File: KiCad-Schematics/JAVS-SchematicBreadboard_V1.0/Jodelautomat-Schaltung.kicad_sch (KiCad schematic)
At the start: 63 parts, among them J1 AudioJack3, J2 I2C_5V_01x04, J4 Screw_Terminal_01x02, J5 USART_Full_01x06, Q1 BC337, Q2 BC337, Q3 BC337, Q4 BC337, Q5 BC337, Q6 BC337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

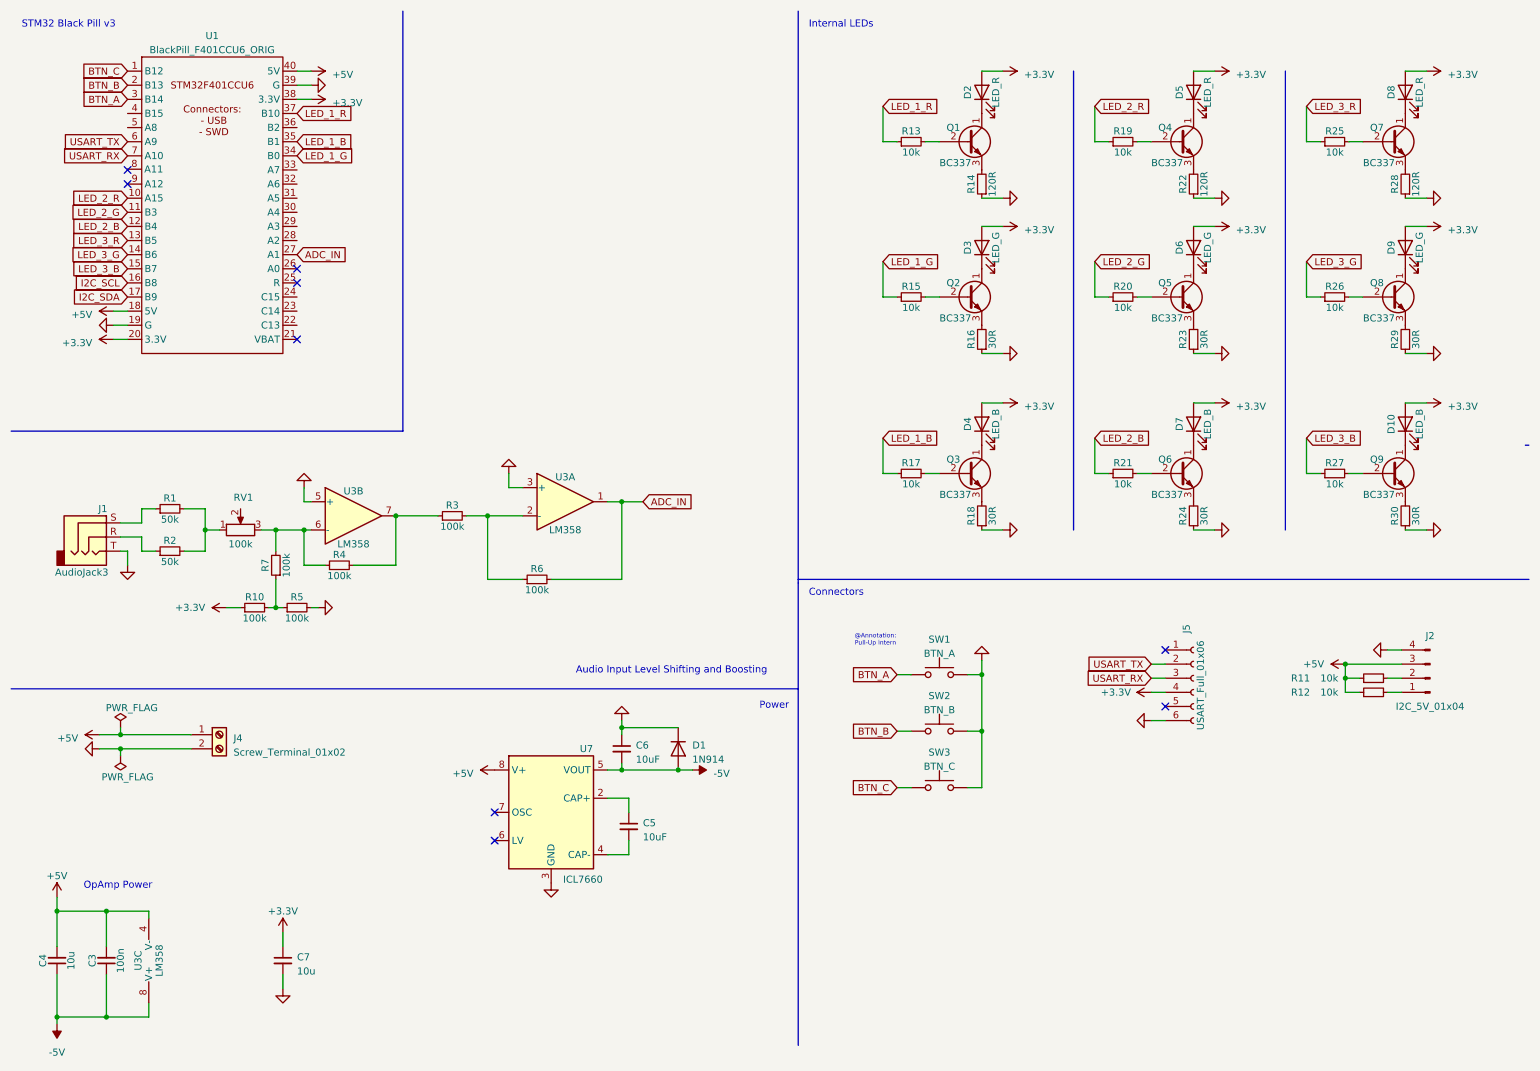
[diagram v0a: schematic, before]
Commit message: some modifications for breadboard creation; removed onboard leds for all stips except strip 1
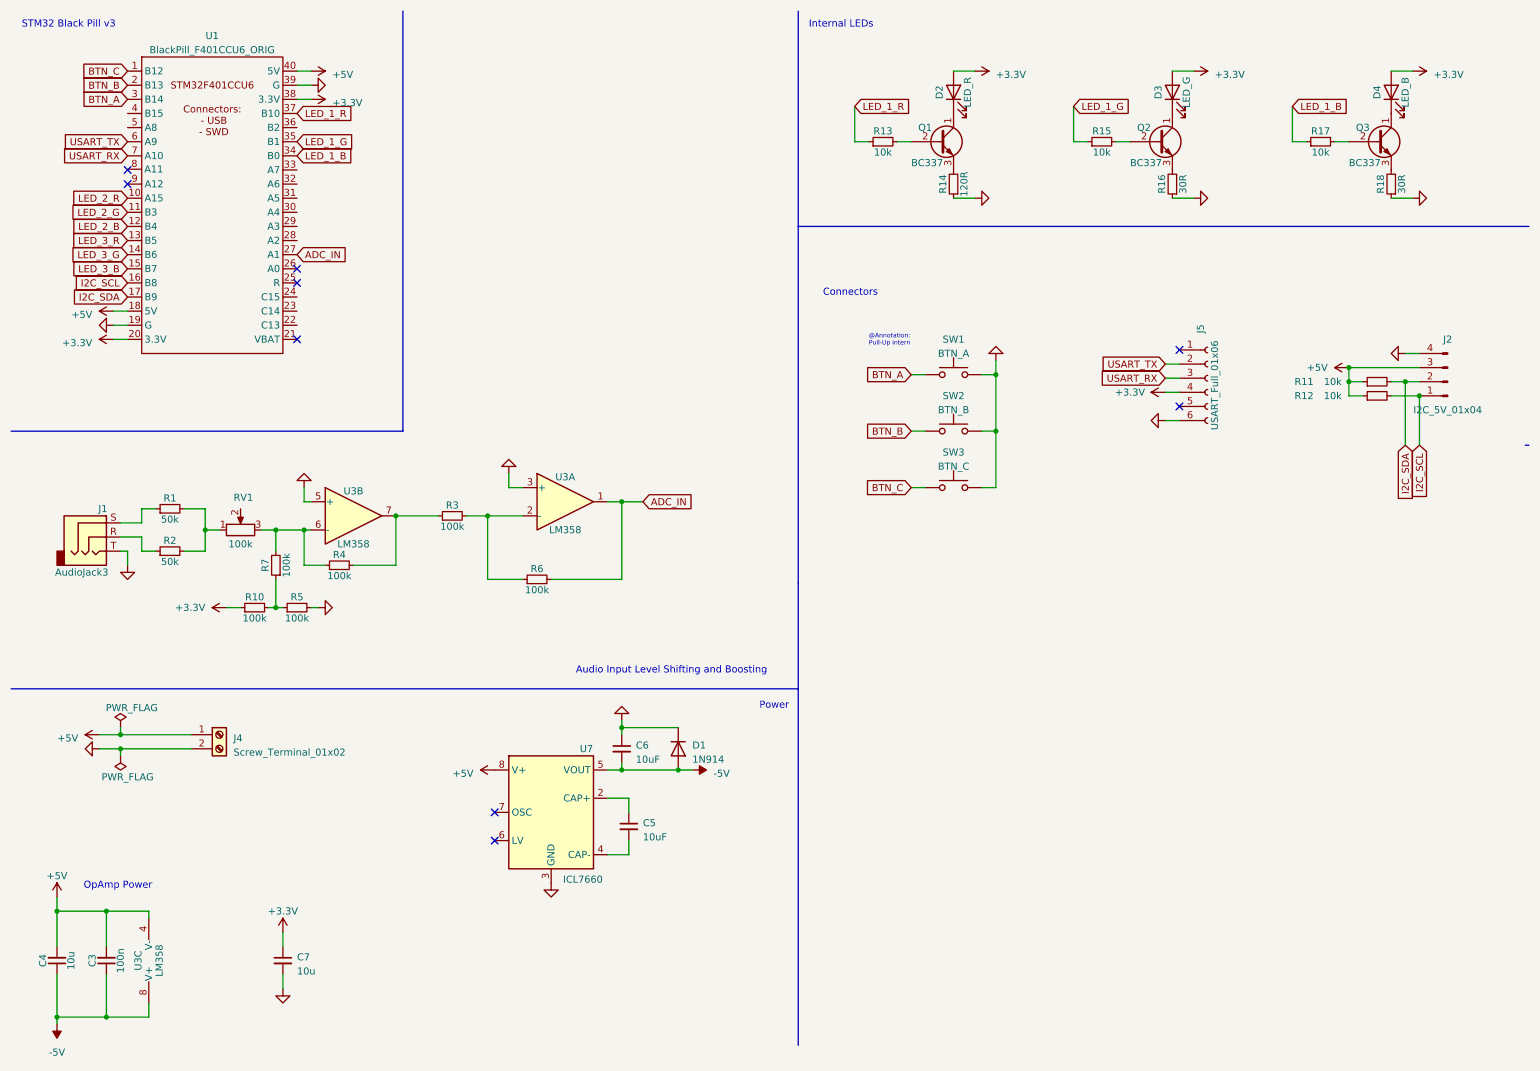
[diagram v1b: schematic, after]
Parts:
- removed D10, D7: LED_B, LED_SMD:LED_2010_5025Metric, symbol Device:LED
- removed D5, D8: LED_R, LED_SMD:LED_2010_5025Metric, symbol Device:LED
- removed D6, D9: LED_G, LED_SMD:LED_2010_5025Metric, symbol Device:LED
- removed Q4, Q5, Q6, Q7, Q8, Q9: BC337, Package_TO_SOT_THT:TO-92_Inline, symbol Transistor_BJT:BC337
- removed R19, R20, R21, R25, R26, R27: 10k, Resistor_SMD:R_0402_1005Metric, symbol Device:R_Small
- removed R22, R28: 120R, Resistor_SMD:R_0603_1608Metric, symbol Device:R_Small
- removed R23, R24, R29, R30: 30R, Resistor_SMD:R_0603_1608Metric, symbol Device:R_Small
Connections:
- net I2C_SCL: now also J2.1 (Pin_1), R12.2
- net I2C_SDA: now also J2.2 (Pin_2), R11.2
- net LED_1_B: now also U1.34 (B0); no longer U1.35 (B1)
- net LED_1_G: now also U1.35 (B1); no longer U1.34 (B0)
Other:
- moved on the sheet: D2, D3, D4, J2, J5, Q1, Q2, Q3, R11, R12, R13, R14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
